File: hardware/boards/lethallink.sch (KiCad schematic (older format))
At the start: 1 part, among them J1 PCIe-x4

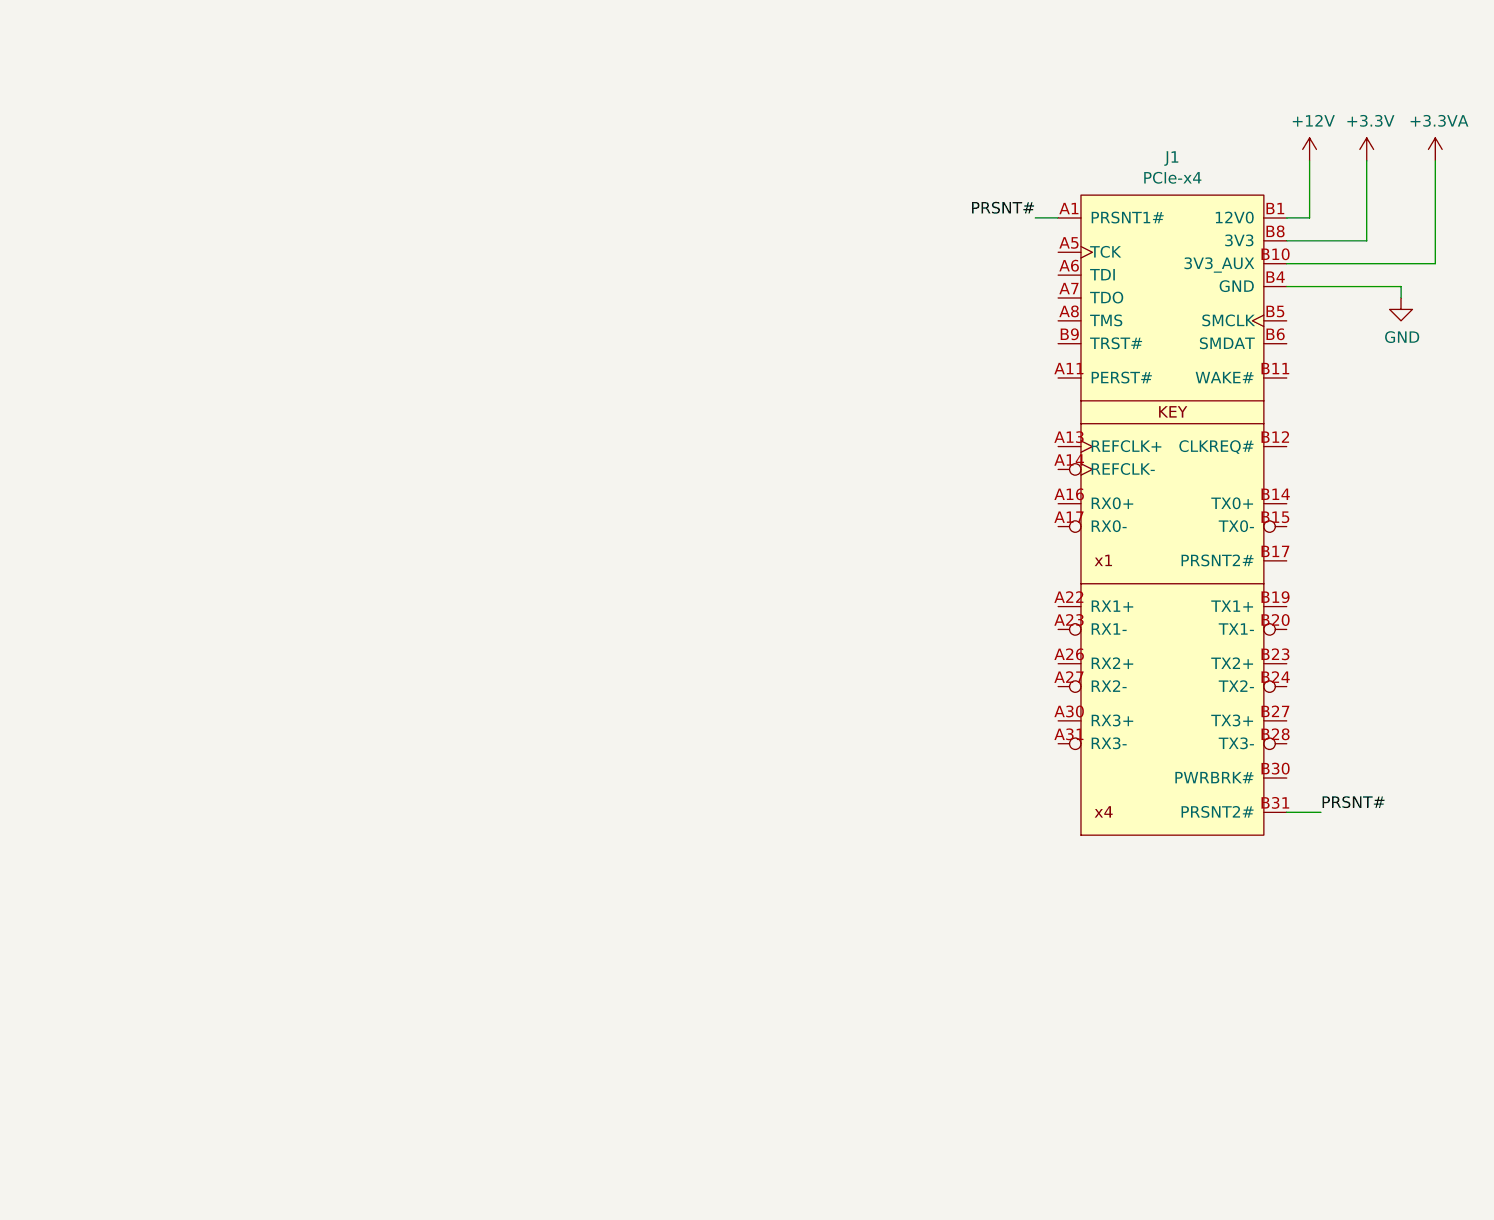
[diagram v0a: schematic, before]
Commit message: Added and hooked up the nested schematic for the FPGA PCIe interface
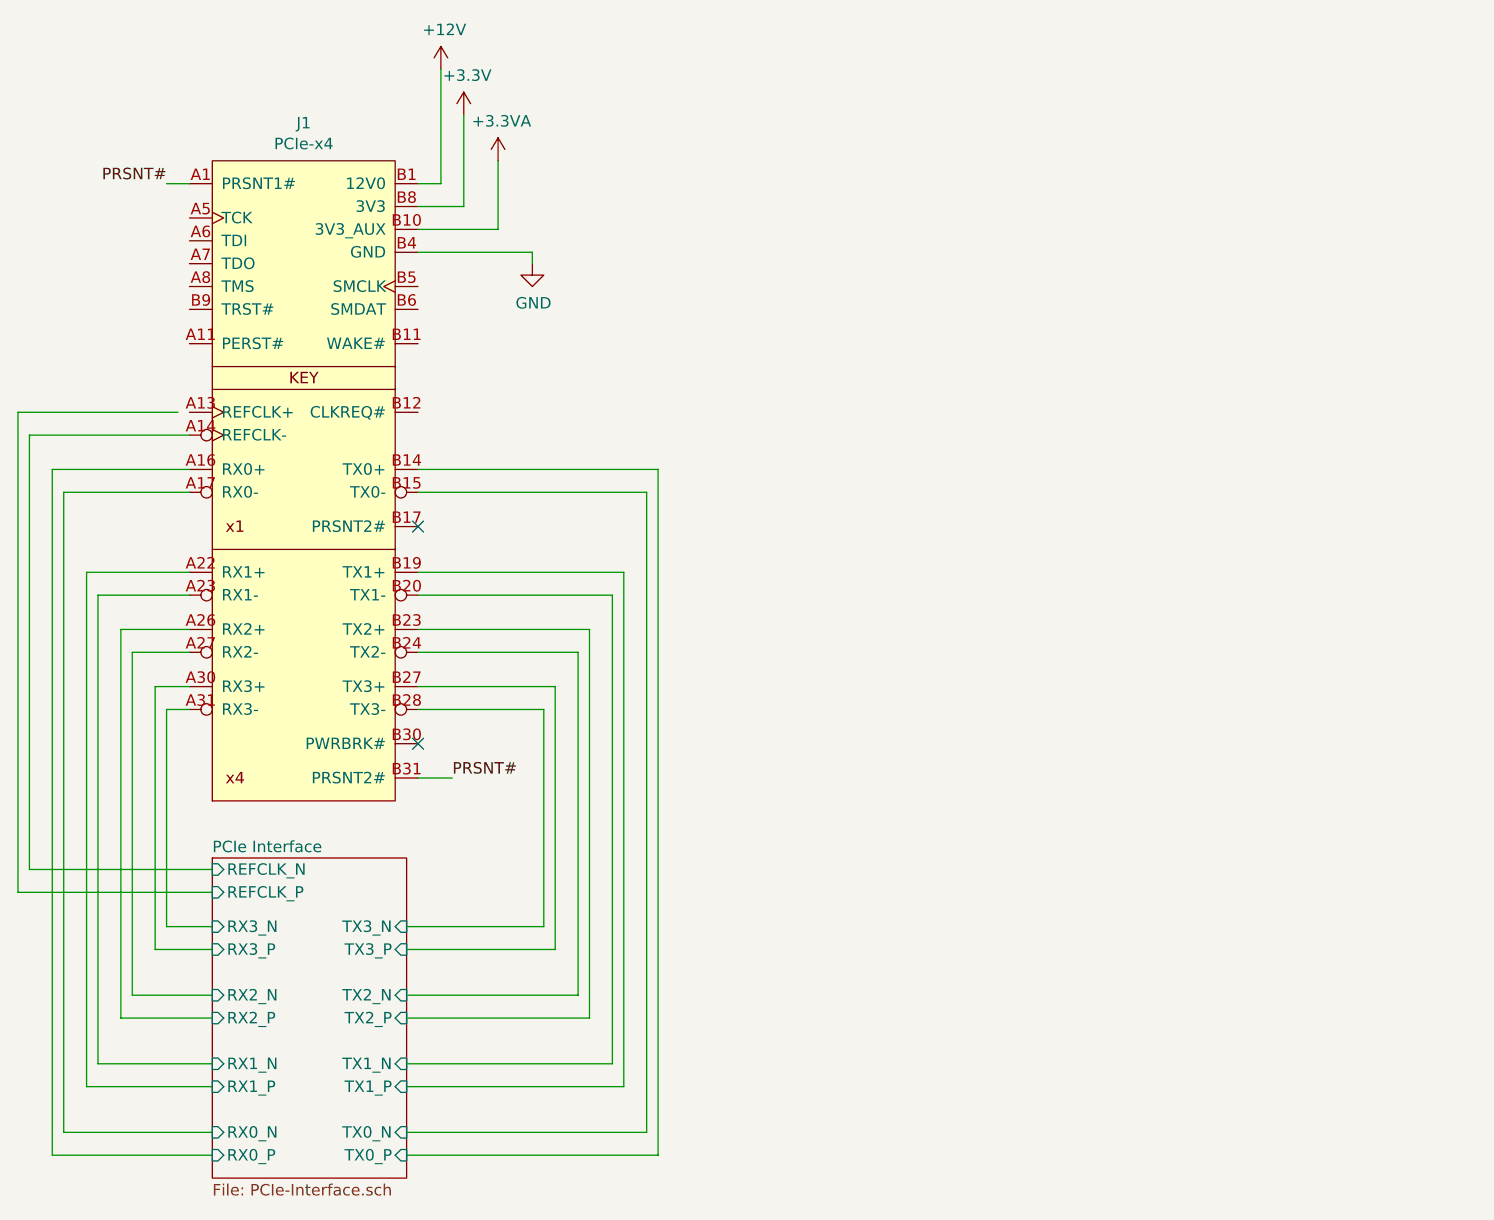
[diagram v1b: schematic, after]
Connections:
- net PCIe Interface/REFCLK_N: now reaches J1.A14 (REFCLK-)
- net PCIe Interface/RX0_P: now reaches J1.A16 (RX0+)
- net PCIe Interface/RX0_N: now reaches J1.A17 (RX0-)
- net PCIe Interface/RX1_P: now reaches J1.A22 (RX1+)
- net PCIe Interface/RX1_N: now reaches J1.A23 (RX1-)
- net PCIe Interface/RX2_P: now reaches J1.A26 (RX2+)
- net PCIe Interface/RX2_N: now reaches J1.A27 (RX2-)
- net PCIe Interface/RX3_P: now reaches J1.A30 (RX3+)
- net PCIe Interface/RX3_N: now reaches J1.A31 (RX3-)
- net PCIe Interface/TX0_P: now reaches J1.B14 (TX0+)
- net PCIe Interface/TX0_N: now reaches J1.B15 (TX0-)
- net PCIe Interface/TX1_P: now reaches J1.B19 (TX1+)
- net PCIe Interface/TX1_N: now reaches J1.B20 (TX1-)
- net PCIe Interface/TX2_P: now reaches J1.B23 (TX2+)
- net PCIe Interface/TX2_N: now reaches J1.B24 (TX2-)
- net PCIe Interface/TX3_P: now reaches J1.B27 (TX3+)
- net PCIe Interface/TX3_N: now reaches J1.B28 (TX3-)
- no-connect marks 0 -> 2
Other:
- moved on the sheet: J1
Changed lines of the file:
@@
 $Descr A4 11693 8268
 encoding utf-8
-Sheet 1 1
+Sheet 1 2
 Title ""
 Date ""
@@
 L lethalbit-pcie:PCIe-x4 J1
 U 1 1 5ED41026
-P 6700 2750
-F 0 "J1" H 6700 3865 50  0000 C CNN
-F 1 "PCIe-x4" H 6700 3774 50  0000 C CNN
-F 2 "lethalbit-pcie:PCIe-x4-Card-FH" H 6850 3850 50  0001 C CNN
-F 3 "" H 6850 3850 50  0001 C CNN
-	1    6700 2750
-	1    0    0    -1
-$EndComp
-Wire Wire Line
-	6200 1900 6100 1900
-Wire Wire Line
-	7200 4500 7350 4500
-Text Label 7350 4500 0    50   ~ 0
+P 2900 2600
+F 0 "J1" H 2900 3715 50  0000 C CNN
+F 1 "PCIe-x4" H 2900 3624 50  0000 C CNN
+F 2 "lethalbit-pcie:PCIe-x4-Card-FH" H 3050 3700 50  0001 C CNN
+F 3 "" H 3050 3700 50  0001 C CNN
+	1    2900 2600
+	1    0    0    -1
+$EndComp
+Wire Wire Line
+	2400 1750 2300 1750
+Wire Wire Line
+	3400 4350 3550 4350
+Text Label 3550 4350 0    50   ~ 0
 PRSNT#
-Text Label 6100 1900 2    50   ~ 0
+Text Label 2300 1750 2    50   ~ 0
 PRSNT#
 $Comp
-L power:GND #PWR?
+L power:GND #PWR0101
 U 1 1 5ED48DF0
-P 7700 2250
-F 0 "#PWR?" H 7700 2000 50  0001 C CNN
-F 1 "GND" H 7705 2077 50  0000 C CNN
-F 2 "" H 7700 2250 50  0001 C CNN
-F 3 "" H 7700 2250 50  0001 C CNN
-	1    7700 2250
-	1    0    0    -1
-$EndComp
-$Comp
-L power:+12V #PWR?
+P 3900 2100
+F 0 "#PWR0101" H 3900 1850 50  0001 C CNN
+F 1 "GND" H 3905 1927 50  0000 C CNN
+F 2 "" H 3900 2100 50  0001 C CNN
+F 3 "" H 3900 2100 50  0001 C CNN
+	1    3900 2100
+	1    0    0    -1
+$EndComp
+$Comp
+L power:+12V #PWR0102
 U 1 1 5ED49518
-P 7300 1650
-F 0 "#PWR?" H 7300 1500 50  0001 C CNN
-F 1 "+12V" H 7315 1823 50  0000 C CNN
-F 2 "" H 7300 1650 50  0001 C CNN
-F 3 "" H 7300 1650 50  0001 C CNN
-	1    7300 1650
-	1    0    0    -1
-$EndComp
-$Comp
-L power:+3.3V #PWR?
+P 3500 1250
+F 0 "#PWR0102" H 3500 1100 50  0001 C CNN
+F 1 "+12V" H 3515 1423 50  0000 C CNN
+F 2 "" H 3500 1250 50  0001 C CNN
+F 3 "" H 3500 1250 50  0001 C CNN
+	1    3500 1250
+	1    0    0    -1
+$EndComp
+$Comp
+L power:+3.3V #PWR0103
 U 1 1 5ED49C5D
-P 7550 1650
-F 0 "#PWR?" H 7550 1500 50  0001 C CNN
-F 1 "+3.3V" H 7565 1823 50  0000 C CNN
-F 2 "" H 7550 1650 50  0001 C CNN
-F 3 "" H 7550 1650 50  0001 C CNN
-	1    7550 1650
-	1    0    0    -1
-$EndComp
-$Comp
-L power:+3.3VA #PWR?
+P 3600 1450
+F 0 "#PWR0103" H 3600 1300 50  0001 C CNN
+F 1 "+3.3V" H 3615 1623 50  0000 C CNN
+F 2 "" H 3600 1450 50  0001 C CNN
+F 3 "" H 3600 1450 50  0001 C CNN
+	1    3600 1450
+	1    0    0    -1
+$EndComp
+$Comp
+L power:+3.3VA #PWR0104
 U 1 1 5ED4A0C8
-P 7850 1650
-F 0 "#PWR?" H 7850 1500 50  0001 C CNN
-F 1 "+3.3VA" H 7865 1823 50  0000 C CNN
-F 2 "" H 7850 1650 50  0001 C CNN
-F 3 "" H 7850 1650 50  0001 C CNN
-	1    7850 1650
-	1    0    0    -1
-$EndComp
-Wire Wire Line
-	7200 1900 7300 1900
-Wire Wire Line
-	7300 1900 7300 1650
-Wire Wire Line
-	7200 2000 7550 2000
-Wire Wire Line
-	7550 2000 7550 1650
-Wire Wire Line
-	7200 2100 7850 2100
-Wire Wire Line
-	7850 2100 7850 1650
-Wire Wire Line
-	7200 2200 7700 2200
-Wire Wire Line
-	7700 2200 7700 2250
+P 3750 1650
+F 0 "#PWR0104" H 3750 1500 50  0001 C CNN
+F 1 "+3.3VA" H 3765 1823 50  0000 C CNN
+F 2 "" H 3750 1650 50  0001 C CNN
+F 3 "" H 3750 1650 50  0001 C CNN
+	1    3750 1650
+	1    0    0    -1
+$EndComp
+Wire Wire Line
+	3400 1750 3500 1750
+Wire Wire Line
+	3500 1750 3500 1250
+Wire Wire Line
+	3400 1850 3600 1850
+Wire Wire Line
+	3600 1850 3600 1450
+Wire Wire Line
+	3400 1950 3750 1950
+Wire Wire Line
+	3750 1950 3750 1650
+Wire Wire Line
+	3400 2050 3900 2050
+Wire Wire Line
+	3900 2050 3900 2100
+$Sheet
+S 2500 4700 850  1400
+U 5ED4B101
+F0 "PCIe Interface" 50
+F1 "PCIe-Interface.sch" 50
+F2 "REFCLK_P" I L 2500 4850 50
+F3 "REFCLK_N" I L 2500 4750 50
+F4 "TX0_P" I R 3350 6000 50
+F5 "TX0_N" I R 3350 5900 50
+F6 "TX1_P" I R 3350 5700 50
+F7 "TX1_N" I R 3350 5600 50
+F8 "TX2_P" I R 3350 5400 50
+F9 "TX2_N" I R 3350 5300 50
+F10 "TX3_P" I R 3350 5100 50
+F11 "TX3_N" I R 3350 5000 50
+F12 "RX0_P" I L 2500 6000 50
+F13 "RX0_N" I L 2500 5900 50
+F14 "RX1_P" I L 2500 5700 50
+F15 "RX1_N" I L 2500 5600 50
+F16 "RX2_P" I L 2500 5400 50
+F17 "RX2_N" I L 2500 5300 50
+F18 "RX3_P" I L 2500 5100 50
+F19 "RX3_N" I L 2500 5000 50
+$EndSheet
+NoConn ~ 3400 4200
+Wire Wire Line
+	2400 4050 2300 4050
+Wire Wire Line
+	2300 4050 2300 5000
+Wire Wire Line
+	2300 5000 2500 5000
+Wire Wire Line
+	2500 5100 2250 5100
+Wire Wire Line
+	2250 5100 2250 3950
+Wire Wire Line
+	2250 3950 2400 3950
+Wire Wire Line
+	2400 3800 2150 3800
+Wire Wire Line
+	2150 3800 2150 5300
+Wire Wire Line
+	2150 5300 2500 5300
+Wire Wire Line
+	2500 5400 2100 5400
+Wire Wire Line
+	2100 5400 2100 3700
+Wire Wire Line
+	2100 3700 2400 3700
+Wire Wire Line
+	2400 3550 2000 3550
+Wire Wire Line
+	2000 3550 2000 5600
+Wire Wire Line
+	2000 5600 2500 5600
+Wire Wire Line
+	2500 5700 1950 5700
+Wire Wire Line
+	1950 5700 1950 3450
+Wire Wire Line
+	1950 3450 2400 3450
+Wire Wire Line
+	2500 5900 1850 5900
+Wire Wire Line
+	1850 5900 1850 3100
+Wire Wire Line
+	1850 3100 2400 3100
+Wire Wire Line
+	2500 6000 1800 6000
+Wire Wire Line
+	1800 6000 1800 3000
+Wire Wire Line
+	1800 3000 2400 3000
+Wire Wire Line
+	2500 4750 1700 4750
+Wire Wire Line
+	1700 4750 1700 2850
+Wire Wire Line
+	1700 2850 2400 2850
+Wire Wire Line
+	2350 2750 1650 2750
+Wire Wire Line
+	1650 2750 1650 4850
+Wire Wire Line
+	1650 4850 2500 4850
+NoConn ~ 3400 3250
+Wire Wire Line
+	3350 5000 3950 5000
+Wire Wire Line
+	3950 4050 3400 4050
+Wire Wire Line
+	3950 5000 3950 4050
+Wire Wire Line
+	3400 3950 4000 3950
+Wire Wire Line
+	4000 3950 4000 5100
+Wire Wire Line
+	4000 5100 3350 5100
+Wire Wire Line
+	3350 5300 4100 5300
+Wire Wire Line
+	4100 5300 4100 3800
+Wire Wire Line
+	4100 3800 3400 3800
+Wire Wire Line
+	3400 3700 4150 3700
+Wire Wire Line
+	4150 3700 4150 5400
+Wire Wire Line
+	4150 5400 3350 5400
+Wire Wire Line
+	3350 5600 4250 5600
+Wire Wire Line
+	4250 5600 4250 3550
+Wire Wire Line
+	4250 3550 3400 3550
+Wire Wire Line
+	3350 5700 4300 5700
+Wire Wire Line
+	4300 5700 4300 3450
+Wire Wire Line
+	4300 3450 3400 3450
+Wire Wire Line
+	3400 3100 4400 3100
+Wire Wire Line
+	4400 3100 4400 5900
+Wire Wire Line
+	4400 5900 3350 5900
+Wire Wire Line
+	3350 6000 4450 6000
+Wire Wire Line
+	4450 6000 4450 3000
+Wire Wire Line
+	4450 3000 3400 3000
 $EndSCHEMATC

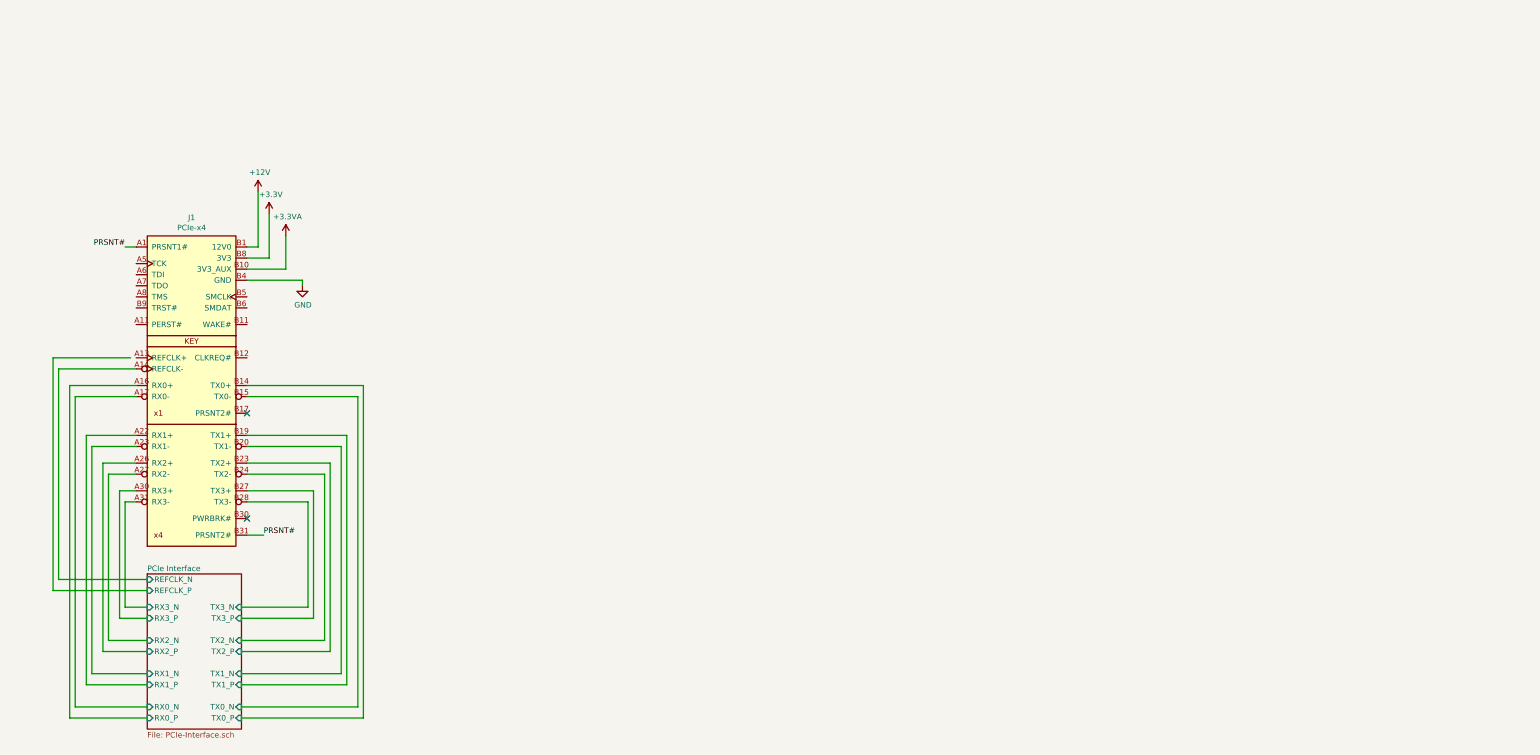
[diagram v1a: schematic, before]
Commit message: Added some more schematics for blocking things out, and tweaked the GND fingers on the PCIe edge a bit
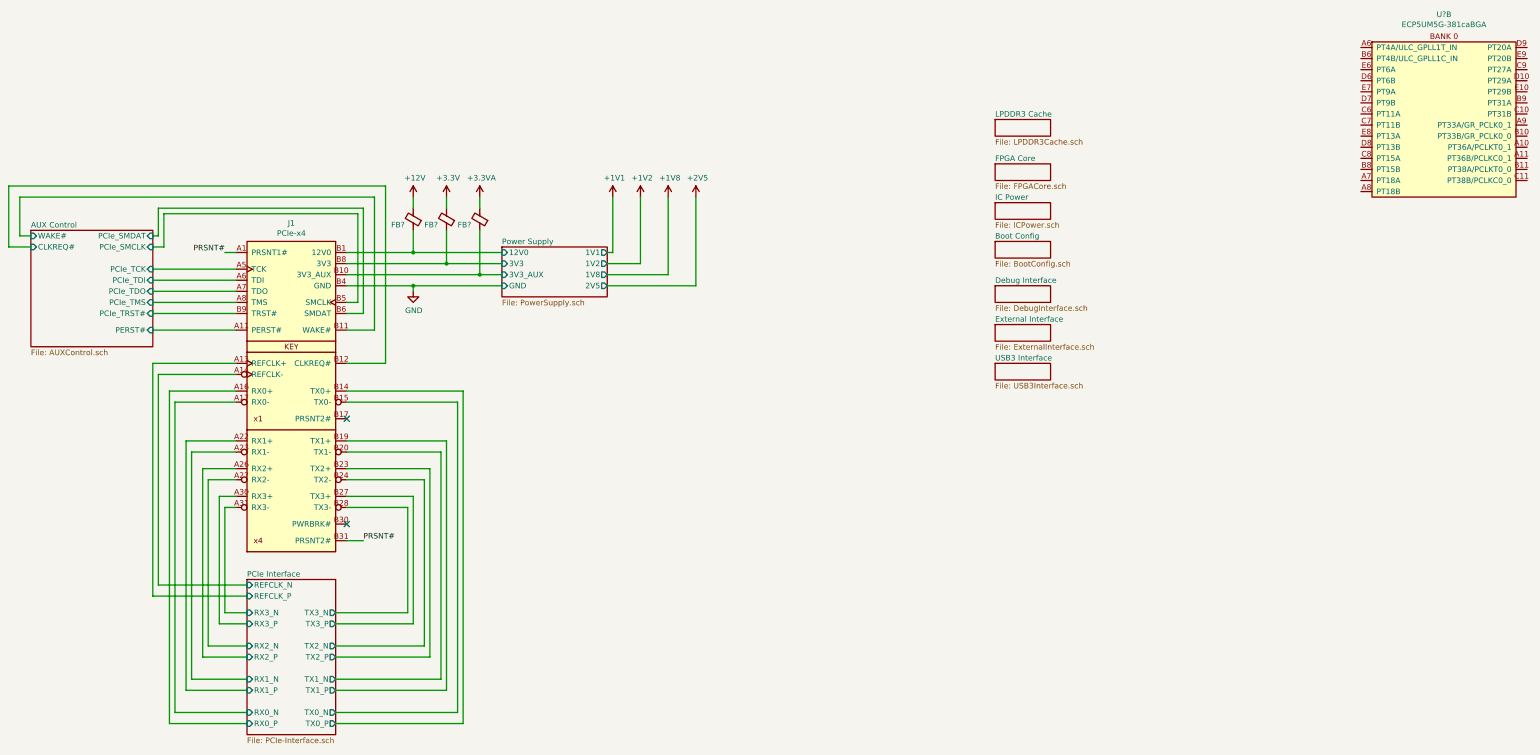
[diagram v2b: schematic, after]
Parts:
- added FB? (x3): Ferrite_Bead_Small, symbol Device:Ferrite_Bead_Small
- added U?: ECP5UM5G-381caBGA, symbol lethalbit:ECP5UM5G-381caBGA
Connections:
- net +12V: now also FB?.2; no longer J1.A2 (12V0), J1.A3 (12V0), J1.B1 (12V0), J1.B2 (12V0), J1.B3 (12V0)
- net +3.3VA: now also FB?.2; no longer J1.B10 (3V3_AUX)
- net +3V3: now also FB?.2; no longer J1.A10 (3V3), J1.A9 (3V3), J1.B8 (3V3)
- net PCIe Interface/REFCLK_P: now also J1.A13 (REFCLK+)
- net AUX Control/PERST#: now reaches J1.A11 (PERST#)
- net AUX Control/PCIe_TCK: now reaches J1.A5 (TCK)
- net AUX Control/PCIe_TDI: now reaches J1.A6 (TDI)
- net AUX Control/PCIe_TDO: now reaches J1.A7 (TDO)
- net AUX Control/PCIe_TMS: now reaches J1.A8 (TMS)
- net AUX Control/WAKE#: now reaches J1.B11 (WAKE#)
- net AUX Control/CLKREQ#: now reaches J1.B12 (CLKREQ#)
- net AUX Control/PCIe_SMCLK: now reaches J1.B5 (SMCLK)
- net AUX Control/PCIe_SMDAT: now reaches J1.B6 (SMDAT)
- net AUX Control/PCIe_TRST#: now reaches J1.B9 (TRST#)
- new net Power Supply/12V0: FB?.1, J1.A2 (12V0), J1.A3 (12V0), J1.B1 (12V0), J1.B2 (12V0), J1.B3 (12V0)
- new net Power Supply/3V3: FB?.1, J1.A10 (3V3), J1.A9 (3V3), J1.B8 (3V3)
- new net Power Supply/3V3_AUX: FB?.1, J1.B10 (3V3_AUX)
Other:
- moved on the sheet: J1
